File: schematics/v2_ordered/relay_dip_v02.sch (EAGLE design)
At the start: 51 parts, among them IC1 74HCT04D, IC2 DS2432P

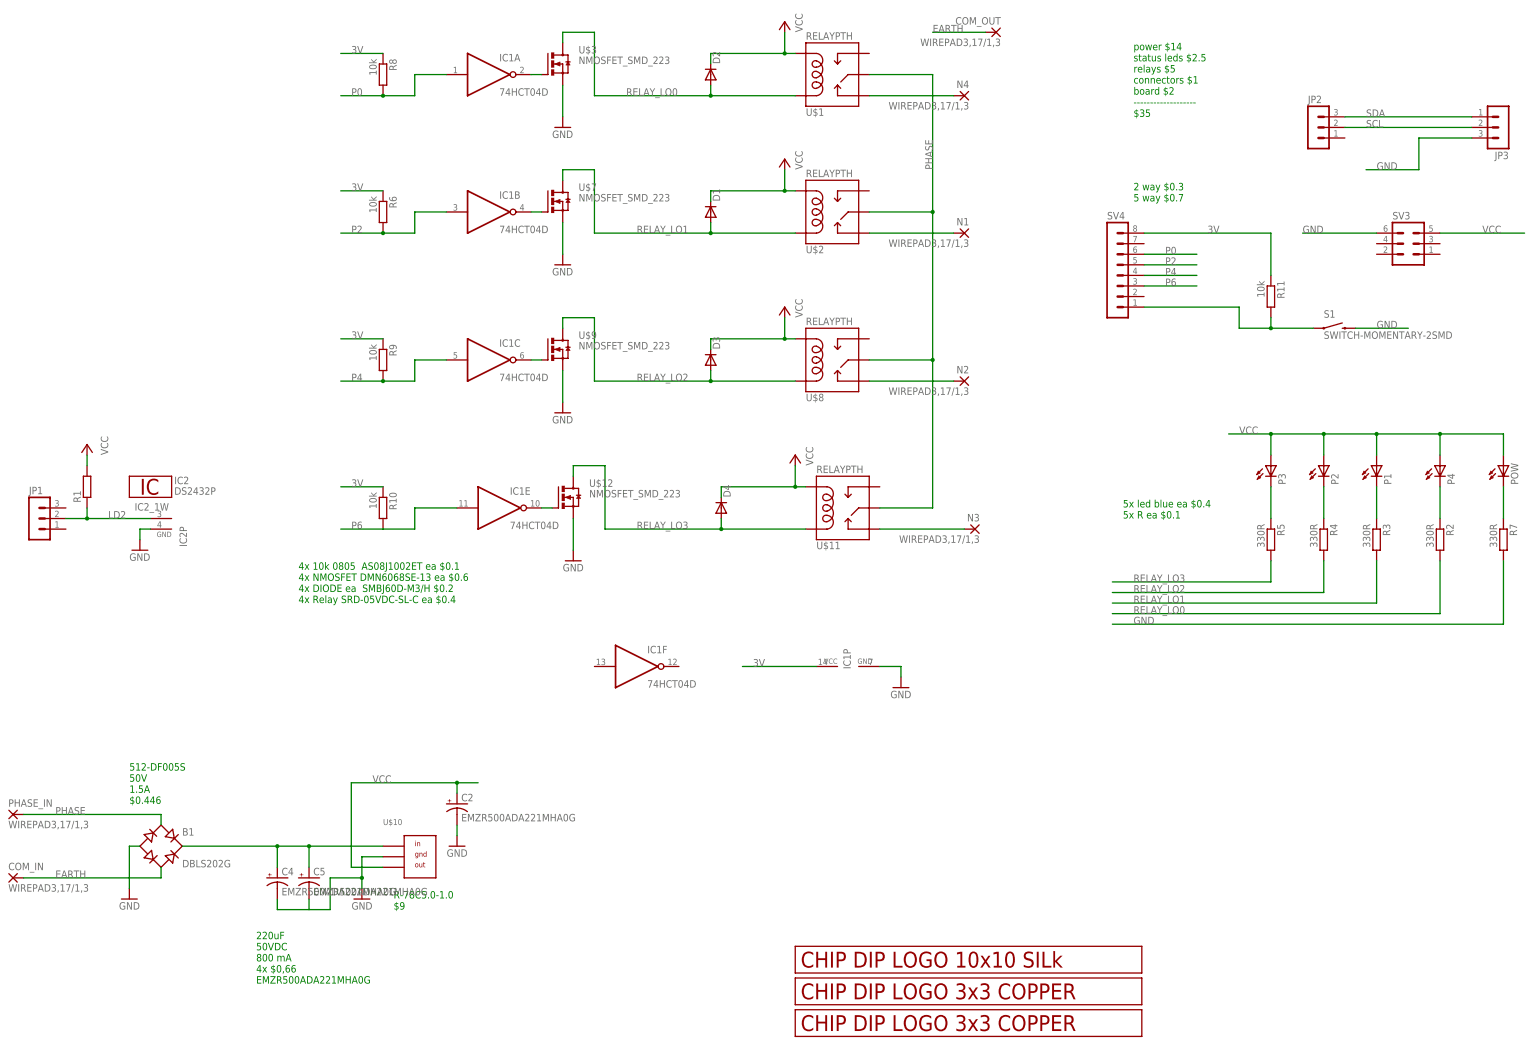
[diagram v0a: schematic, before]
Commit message: added v3, fixed ds2431 footprint, added quotation
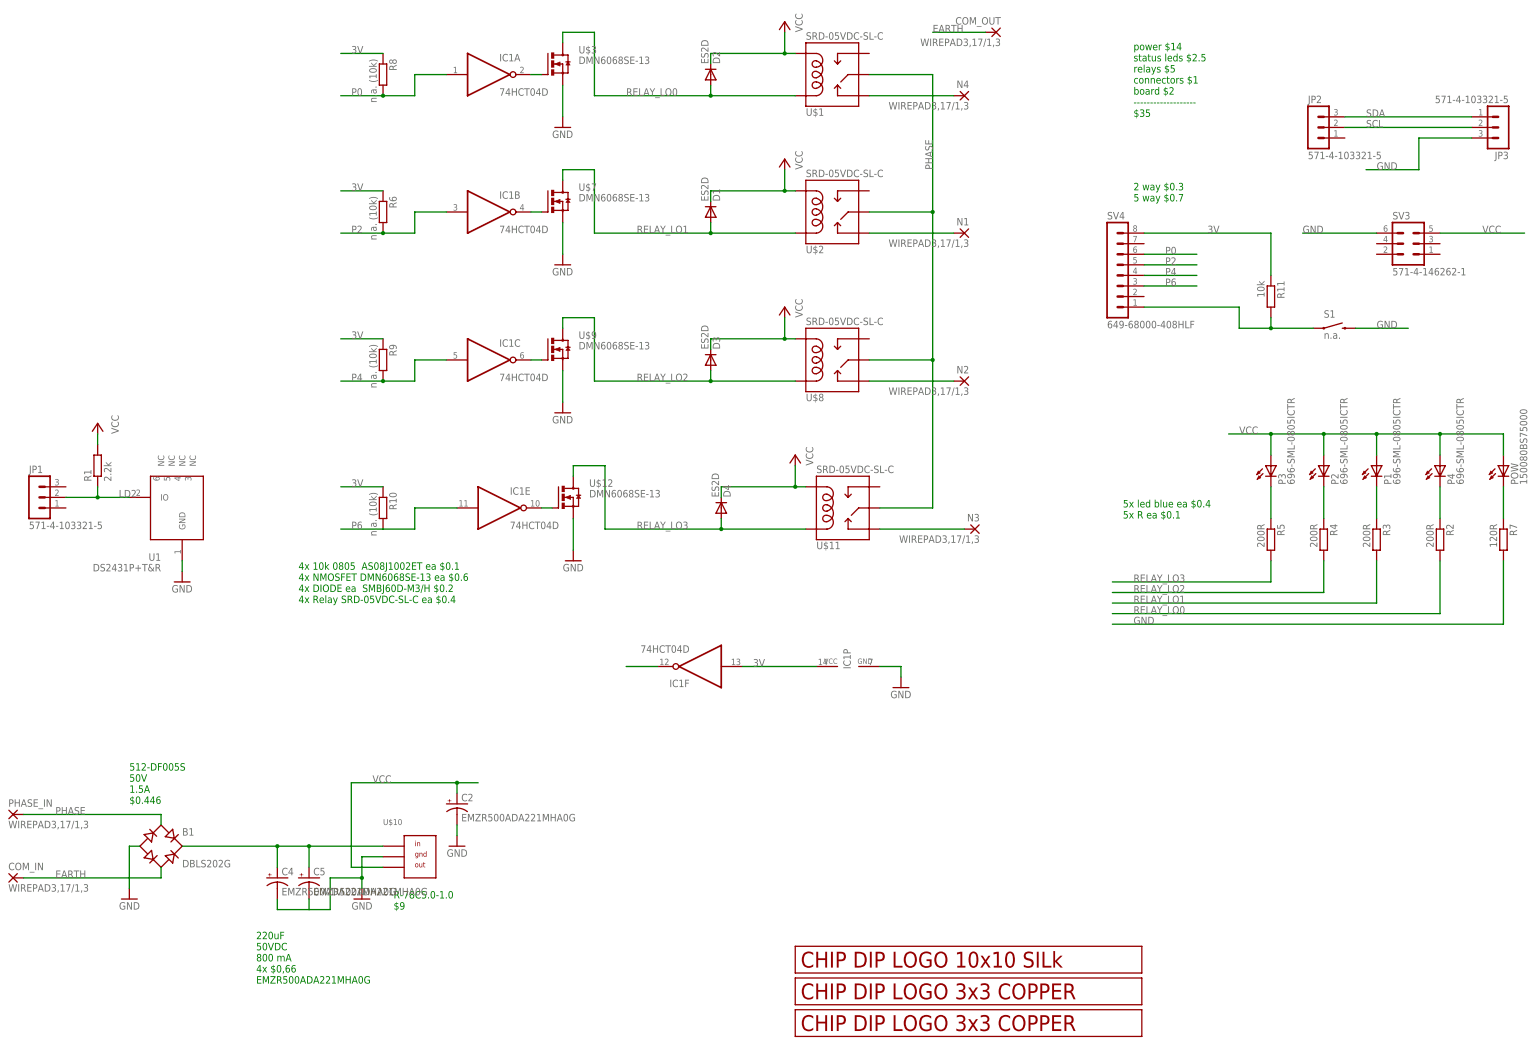
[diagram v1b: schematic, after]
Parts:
- removed IC2: DS2432P, 1wire:DS2432P
- added U1: DS2431P+T&R, JKW_CHIP:DS2431P
- D1, D2, D3, D4: value (none) -> ES2D
- JP1, JP2, JP3: value (none) -> 571-4-103321-5
- P1, P2, P3, P4: value (none) -> 696-SML-0805ICTR
- POW: value (none) -> 150080BS75000
- R1: value (none) -> 2.2k
- R10, R6, R8, R9: value 10k -> n.a. (10k)
- R2, R3, R4, R5: value 330R -> 200R
- R7: value 330R -> 120R
- S1: value SWITCH-MOMENTARY-2SMD -> n.a.
- SV3: value (none) -> 571-4-146262-1
- SV4: value (none) -> 649-68000-408HLF
- U$1, U$11, U$2, U$8: value RELAYPTH -> SRD-05VDC-SL-C
- U$12, U$3, U$7, U$9: value NMOSFET_SMD_223 -> DMN6068SE-13
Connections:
- new net N$6: IC1F.O
- net 3V: now also IC1F.I
- net GND: now also U1.GND; no longer IC2P.GND
- net LD2: now also U1.IO; no longer IC2_1W.1W
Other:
- moved on the sheet: IC1F, JP1, R1
